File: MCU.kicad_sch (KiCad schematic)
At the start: 7 parts, among them J1 Conn_ARM_SWD_TagConnect_TC203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, U1 NORA-B106-00B, Y2 CLK_0002

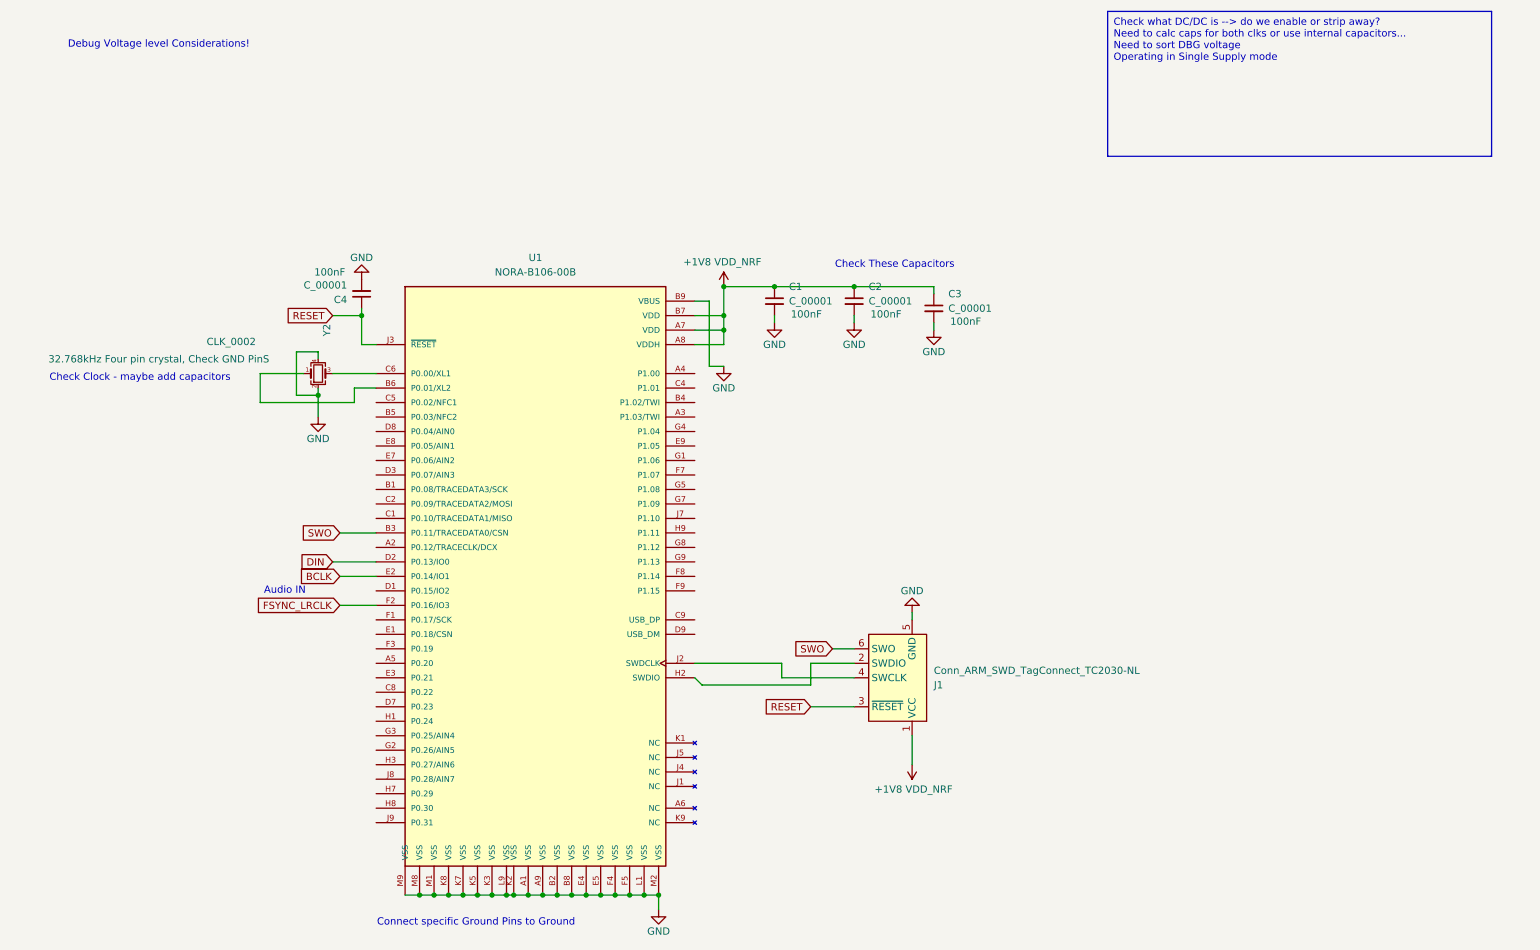
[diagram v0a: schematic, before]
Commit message: routed pins for SD card
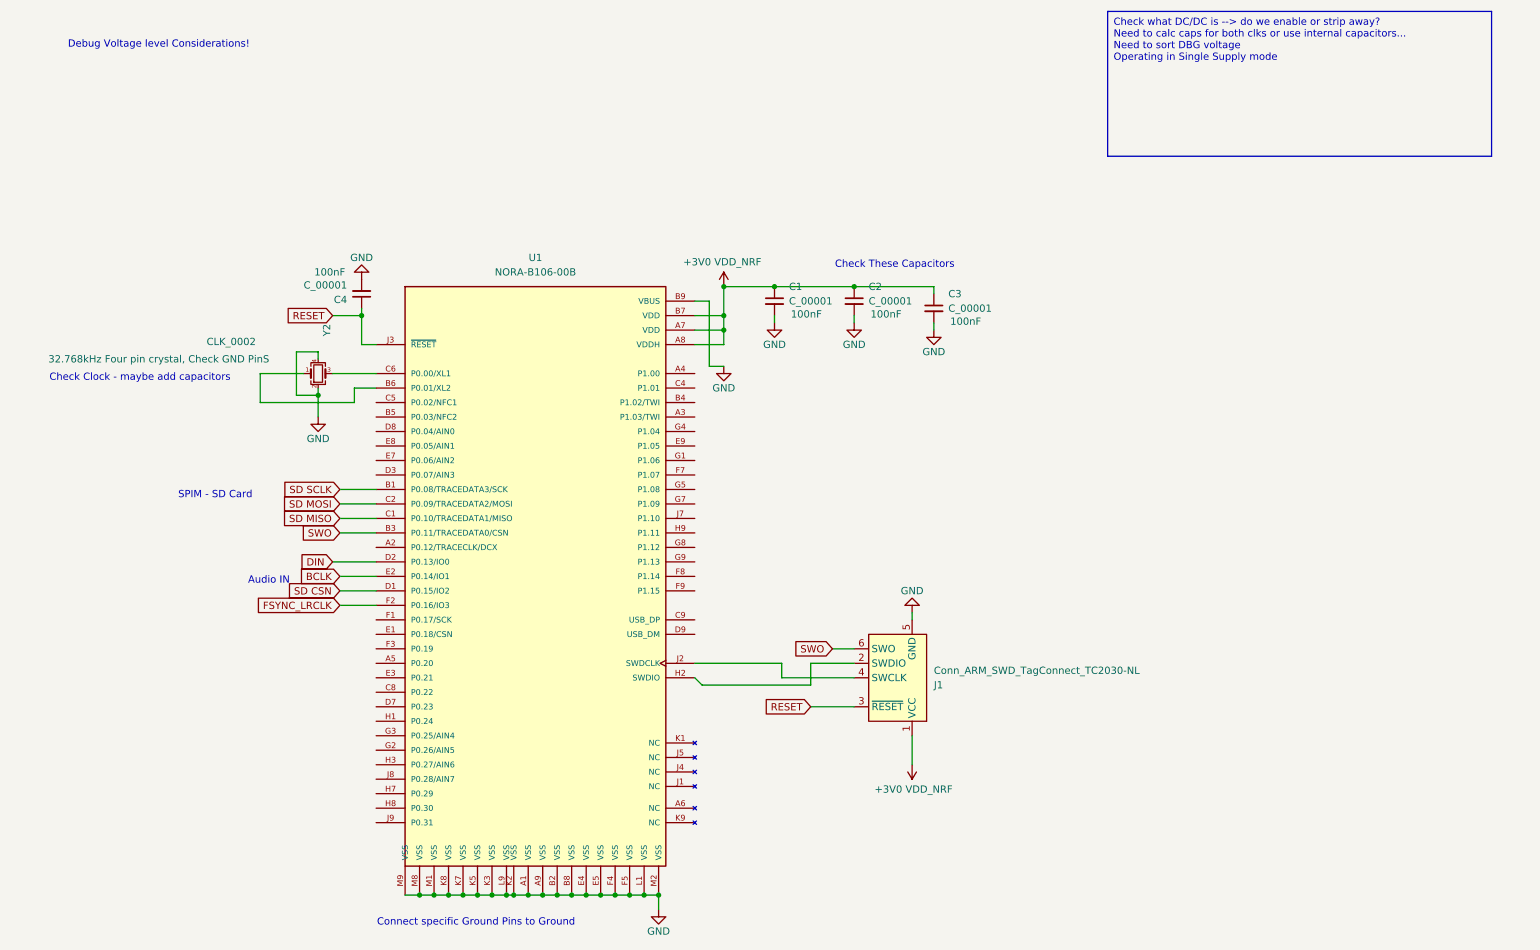
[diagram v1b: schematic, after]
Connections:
- net SD SCLK: now reaches U1.B1 (P0.08/TRACEDATA3/SCK)
- net SD MISO: now reaches U1.C1 (P0.10/TRACEDATA1/MISO)
- net SD MOSI: now reaches U1.C2 (P0.09/TRACEDATA2/MOSI)
- net SD CSN: now reaches U1.D1 (P0.15/IO2)
- net +1V8 VDD_NRF renamed +3V0 VDD_NRF
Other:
- note added: "SPIM - SD Card"
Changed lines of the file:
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@@
+	(wire
+		(pts
+			(xy 80.01 101.6) (xy 86.36 101.6)
+		)
+		(stroke
+			(width 0)
+			(type default)
+		)
+	)
 	(wire
 		(pts
@@
 	(wire
 		(pts
+			(xy 80.01 116.84) (xy 86.36 116.84)
+		)
+		(stroke
+			(width 0)
+			(type default)
+		)
+	)
+	(wire
+		(pts
 			(xy 80.01 119.38) (xy 86.36 119.38)
 		)
@@
 	(wire
 		(pts
+			(xy 80.01 99.06) (xy 86.36 99.06)
+		)
+		(stroke
+			(width 0)
+			(type default)
+		)
+	)
+	(wire
+		(pts
 			(xy 120.65 170.18) (xy 123.19 170.18)
 		)
@@
 		(pts
 			(xy 123.19 170.18) (xy 125.73 170.18)
+		)
+		(stroke
+			(width 0)
+			(type default)
+		)
+	)
+	(wire
+		(pts
+			(xy 80.01 104.14) (xy 86.36 104.14)
 		)
 		(stroke
@@
 		)
 	)
+	(text "SPIM - SD Card"
+		(exclude_from_sim no)
+		(at 58.166 100.076 0)
+		(effects
+			(font
+				(size 1.27 1.27)
+			)
+		)
+	)
 	(text "Audio IN"
 		(exclude_from_sim no)
-		(at 70.358 116.84 0)
+		(at 67.564 115.062 0)
 		(effects
 			(font
@@
 			(font
 				(size 1.27 1.27)
+			)
+		)
+	)
+	(global_label "SD MOSI"
+		(shape input)
+		(at 80.01 101.6 180)
+		(fields_autoplaced yes)
+		(effects
+			(font
+				(size 1.27 1.27)
+			)
+			(justify right)
+		)
+		(property "Intersheetrefs" "${INTERSHEET_REFS}"
+			(at 68.9815 101.6 0)
+			(effects
+				(font
+					(size 1.27 1.27)
+				)
+				(justify right)
+				(hide yes)
 			)
 		)
@@
 		)
 	)
+	(global_label "SD MISO"
+		(shape input)
+		(at 80.01 104.14 180)
+		(fields_autoplaced yes)
+		(effects
+			(font
+				(size 1.27 1.27)
+			)
+			(justify right)
+		)
+		(property "Intersheetrefs" "${INTERSHEET_REFS}"
+			(at 68.9815 104.14 0)
+			(effects
+				(font
+					(size 1.27 1.27)
+				)
+				(justify right)
+				(hide yes)
+			)
+		)
+	)
 	(global_label "BCLK"
 		(shape input)
@@
 		)
 	)
+	(global_label "SD CSN"
+		(shape input)
+		(at 80.01 116.84 180)
+		(fields_autoplaced yes)
+		(effects
+			(font
+				(size 1.27 1.27)
+			)
+			(justify right)
+		)
+		(property "Intersheetrefs" "${INTERSHEET_REFS}"
+			(at 69.7677 116.84 0)
+			(effects
+				(font
+					(size 1.27 1.27)
+				)
+				(justify right)
+				(hide yes)
+			)
+		)
+	)
 	(global_label "FSYNC_LRCLK"
 		(shape input)
@@
 		(property "Intersheetrefs" "${INTERSHEET_REFS}"
 			(at 64.2038 119.38 0)
+			(effects
+				(font
+					(size 1.27 1.27)
+				)
+				(justify right)
+				(hide yes)
+			)
+		)
+	)
+	(global_label "SD SCLK"
+		(shape input)
+		(at 80.01 99.06 180)
+		(fields_autoplaced yes)
+		(effects
+			(font
+				(size 1.27 1.27)
+			)
+			(justify right)
+		)
+		(property "Intersheetrefs" "${INTERSHEET_REFS}"
+			(at 68.8001 99.06 0)
 			(effects
 				(font
@@
 			)
 		)
-		(property "Value" "+1V8 VDD_NRF"
+		(property "Value" "+3V0 VDD_NRF"
 			(at 147.066 59.182 0)
 			(effects
@@
 			)
 		)
-		(property "Value" "+1V8 VDD_NRF"
+		(property "Value" "+3V0 VDD_NRF"
 			(at 180.594 151.638 0)
 			(effects

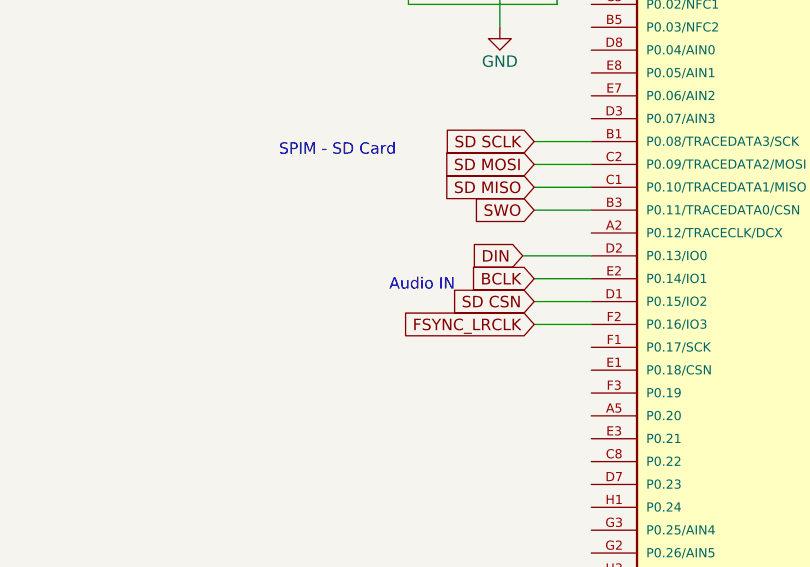
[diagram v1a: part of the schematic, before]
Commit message: Added pull ups to SD data lines in line with SD standard
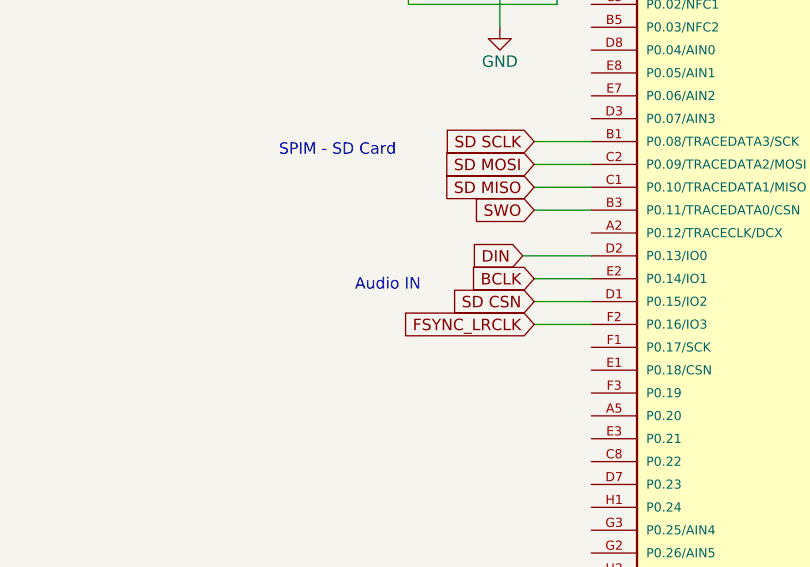
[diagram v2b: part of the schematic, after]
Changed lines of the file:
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@@
 	(text "Audio IN"
 		(exclude_from_sim no)
-		(at 67.564 115.062 0)
+		(at 63.754 115.062 0)
 		(effects
 			(font

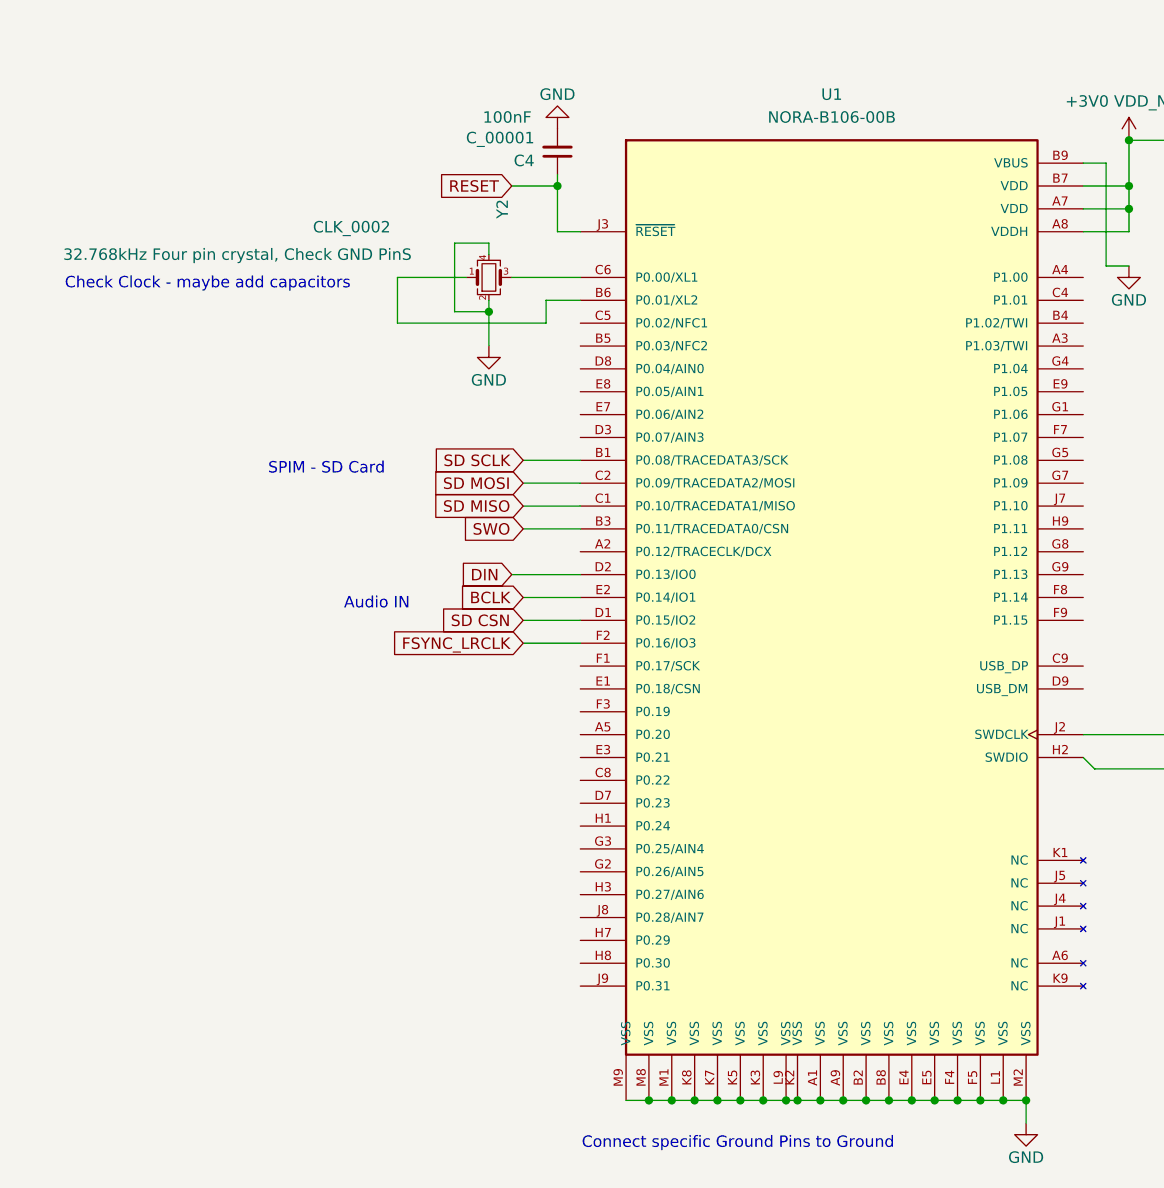
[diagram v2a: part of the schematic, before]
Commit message: added two active high push buttons
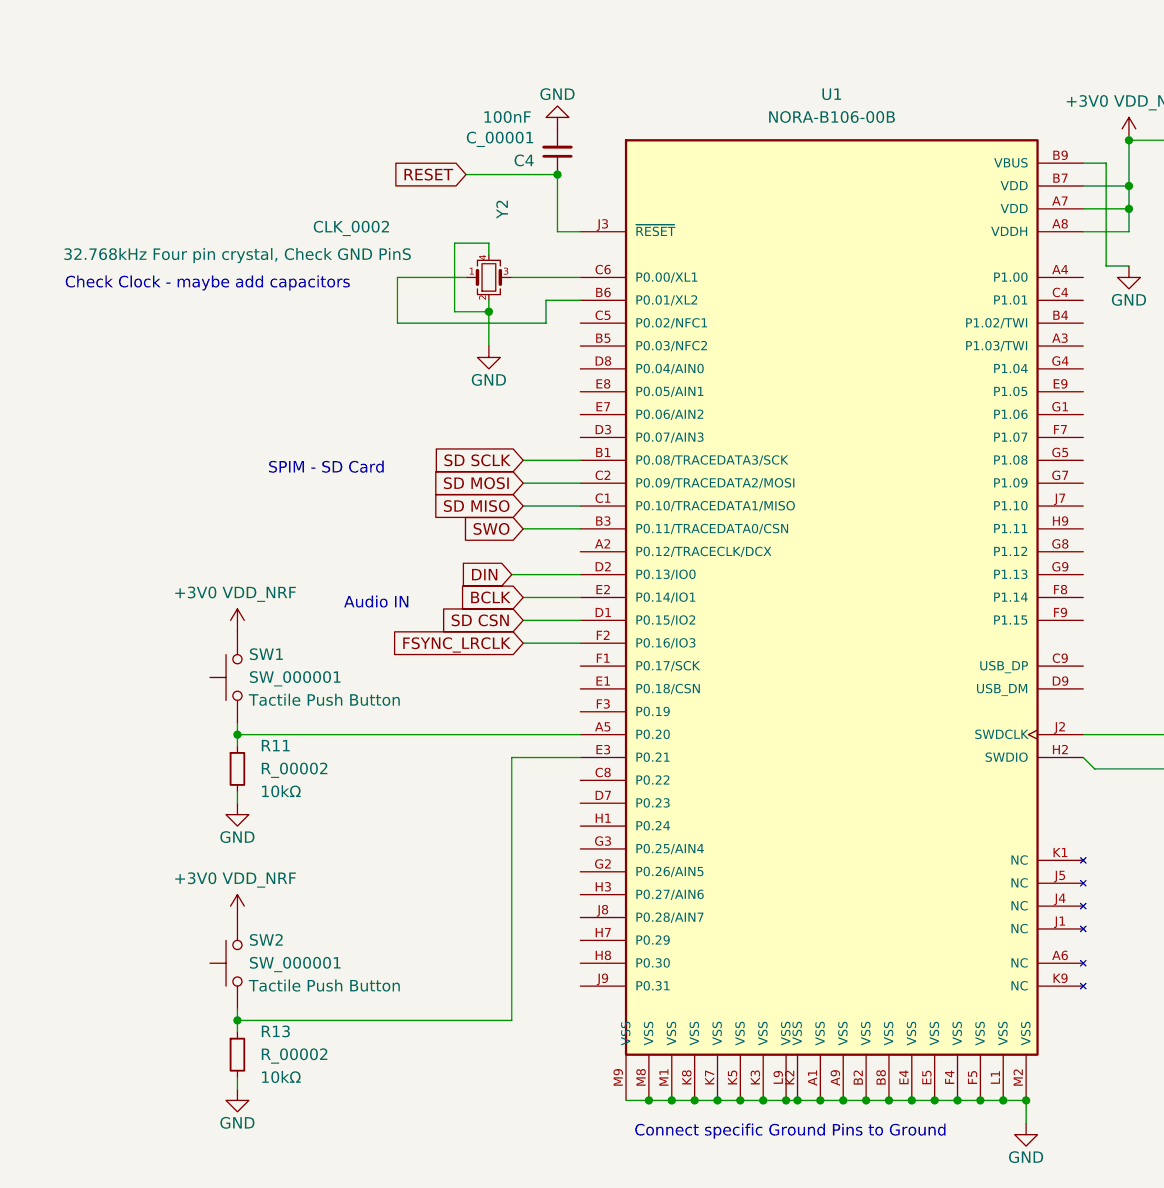
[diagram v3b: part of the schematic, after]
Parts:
- added R11, R13: R_00002, symbol mic_patch_parts:R_00003
- added SW1, SW2: SW_000001, symbol mic_patch_parts:SW_000001
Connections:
- net +3V0 VDD_NRF: now also SW1.2, SW2.2
- net GND: now also R11.2, R13.2
- net at U1.A5 (P0.20): now also R11.1, SW1.1
- net at U1.E3 (P0.21): now also R13.1, SW2.1

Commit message: changed vterm to 4.25V on the npm1100, added GPIO control of npm1100 BUCK modes
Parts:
- added D3: LED_0002, symbol mic_patch_parts:LED_0003
- added R14: R_00002, symbol mic_patch_parts:R_00003
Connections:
- net GND: now also R14.2
- net NPM MODE: now reaches U1.E9 (P1.05)
- net NPM ERROR: now reaches U1.G4 (P1.04)
- net at U1.J7 (P1.10): now also D3.2 (A)
- new net: D3.1 (K), R14.1
- no-connect marks 0 -> 35
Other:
- note added: "Change resistor depending on LED"

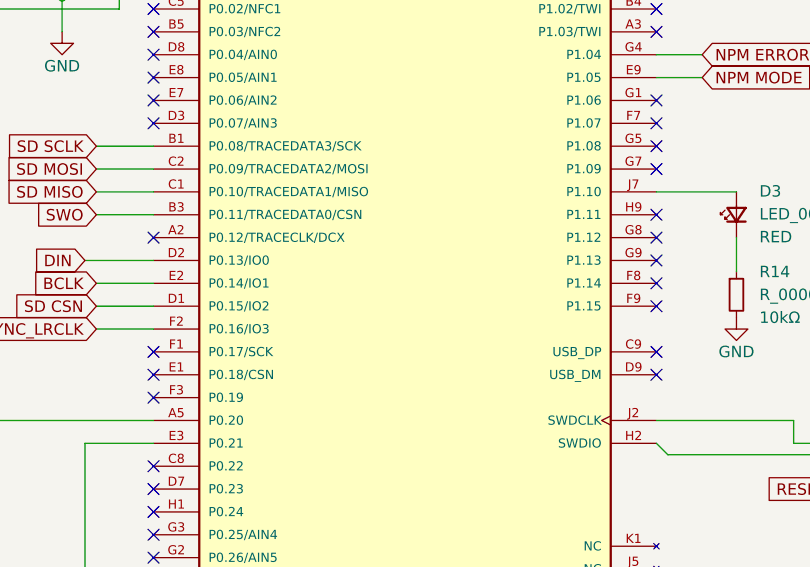
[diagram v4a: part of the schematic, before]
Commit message: added symbol, 3D model and footprint for nora ble module
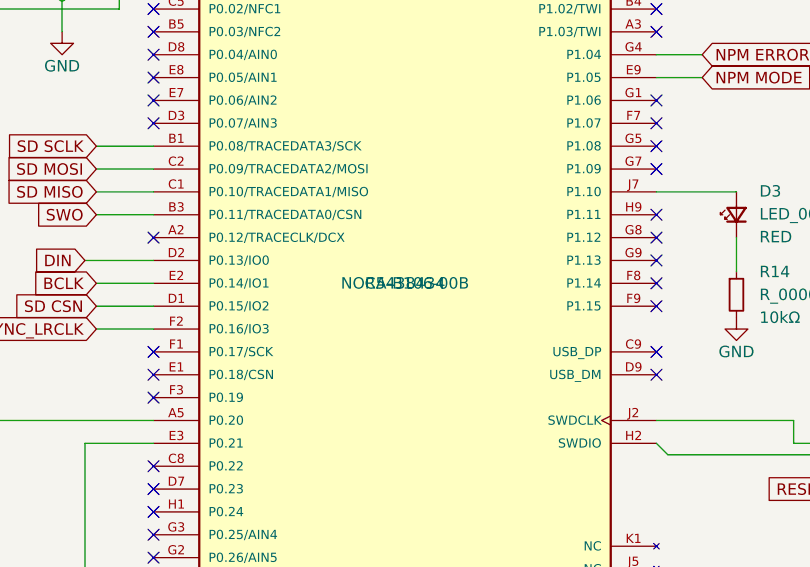
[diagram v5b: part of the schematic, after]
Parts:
- U1: footprint NORA-B106-00B:XCVR_NORA-B106-00B -> mic_patch_parts:NORA-B106-00B; LCSC PNs (none) -> C5438434; MPNS (none) -> NORA-B106-00B
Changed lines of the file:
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@@
 			)
 		)
-		(property "Footprint" "NORA-B106-00B:XCVR_NORA-B106-00B"
+		(property "Footprint" "mic_patch_parts:NORA-B106-00B"
 			(at 114.3 114.3 0)
 			(effects
@@
 			)
 		)
-		(property "Datasheet" ""
+		(property "Datasheet" "https://content.u-blox.com/sites/default/files/NORA-B1_DataSheet_UBX-20027119.pdf?utm_content=UBX-20027119"
 			(at 114.3 114.3 0)
 			(effects
@@
 			)
 		)
-		(property "Description" ""
+		(property "Description" "Nora B106 NRF5340 BLE Module PCB Ant"
 			(at 114.3 114.3 0)
 			(effects
@@
 			)
 		)
+		(property "MPNS" "NORA-B106-00B"
+			(at 114.3 114.3 0)
+			(effects
+				(font
+					(size 1.27 1.27)
+				)
+			)
+		)
+		(property "LCSC PNs" "C5438434"
+			(at 114.3 114.3 0)
+			(effects
+				(font
+					(size 1.27 1.27)
+				)
+			)
+		)
